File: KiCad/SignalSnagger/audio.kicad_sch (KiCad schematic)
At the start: 36 parts, among them J301 AudioJack4, U301 LM386, U302 LT6231

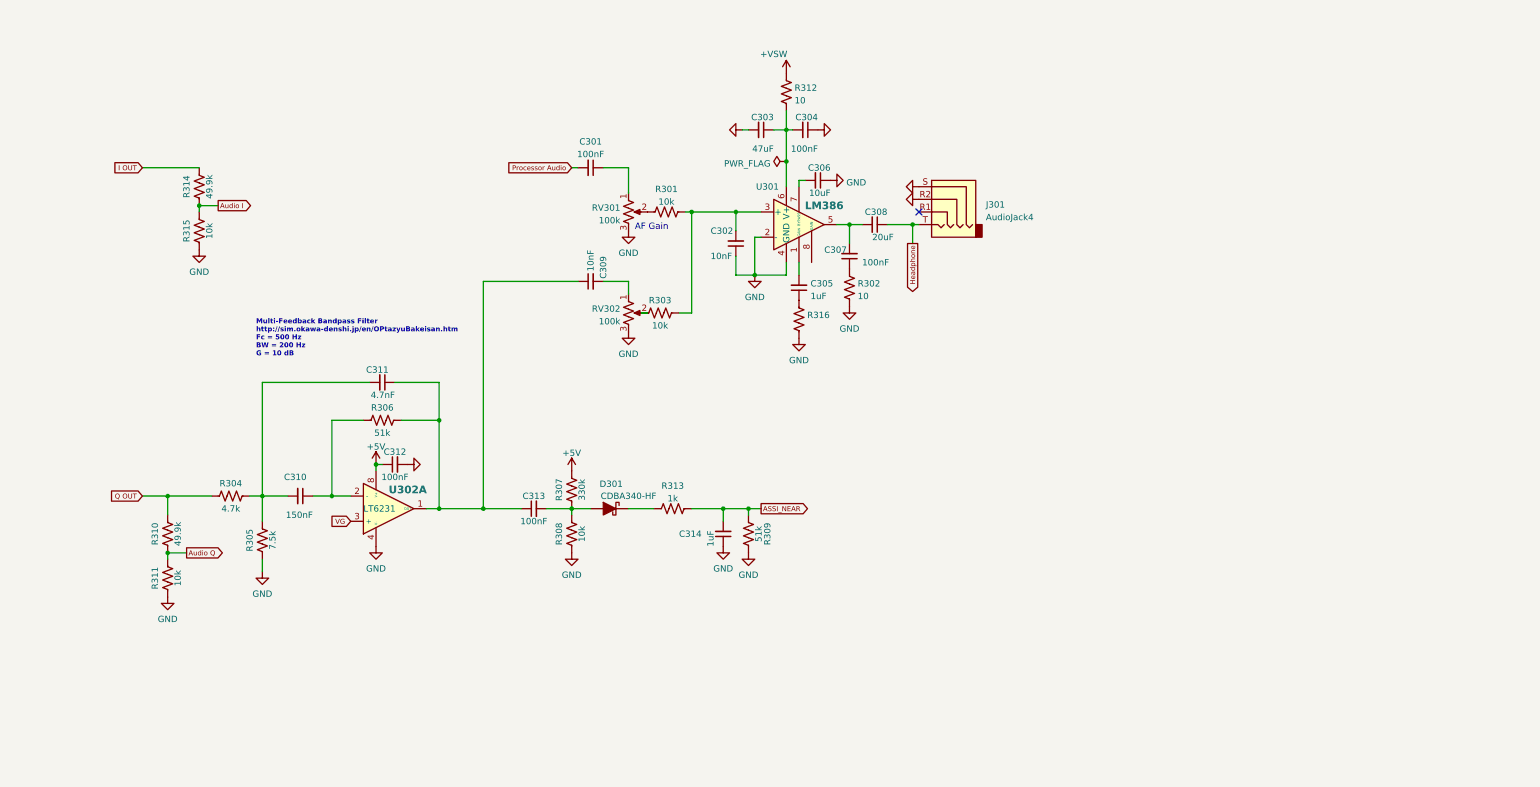
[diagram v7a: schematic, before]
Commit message: Stereo Support
Updates to Audio schematic to reflect discussions regarding stereo support.
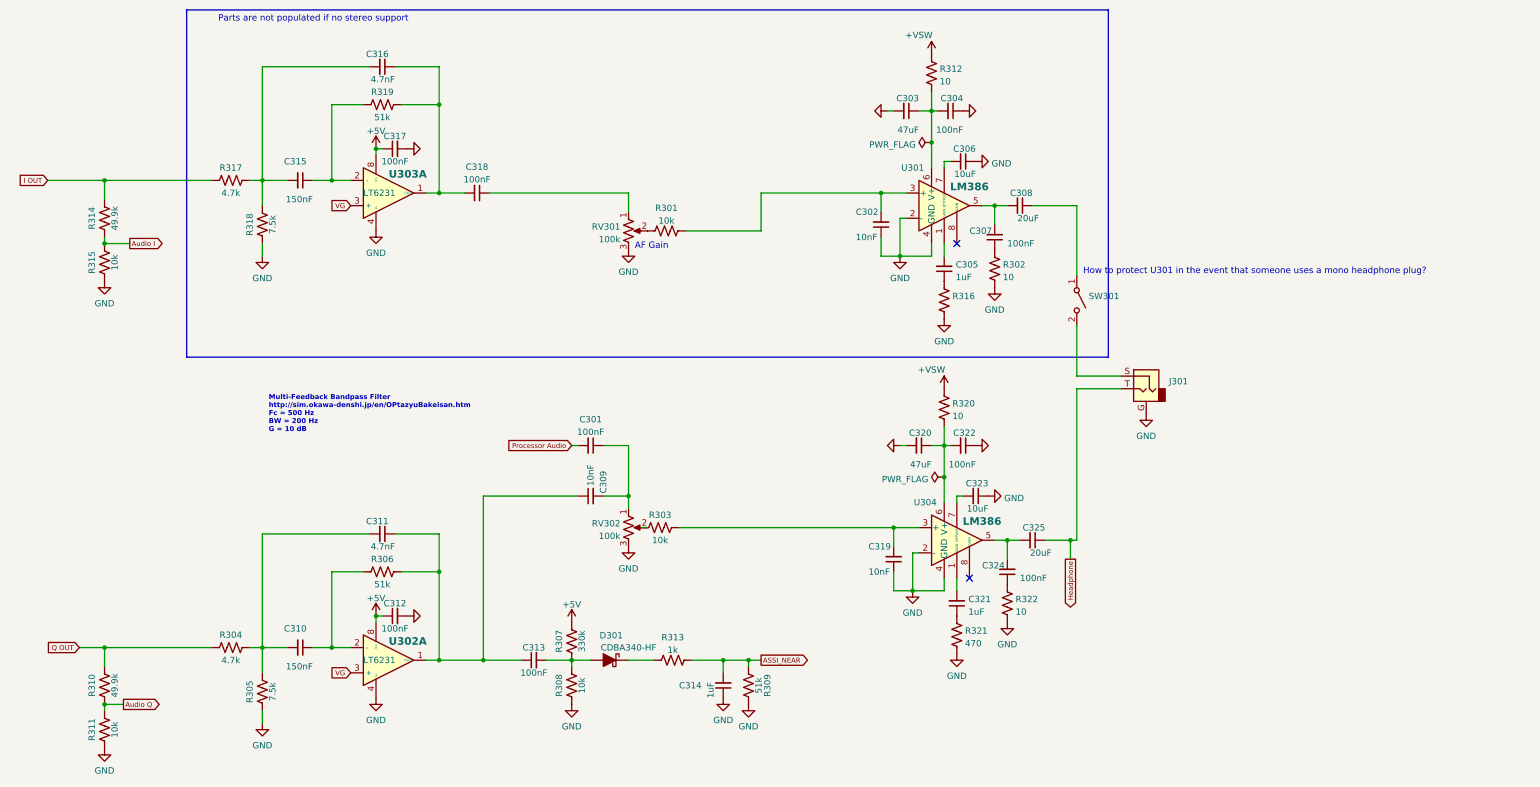
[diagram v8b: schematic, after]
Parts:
- removed J301: AudioJack4, symbol Connector:AudioJack4
- added C315: 150nF, symbol Device:C_Small
- added C316: 4.7nF, symbol Device:C_Small
- added C317, C318, C322, C324: 100nF, symbol Device:C_Small
- added C319: 10nF, symbol Device:C_Small
- added C320: 47uF, symbol Device:C_Small
- added C321: 1uF, symbol Device:C_Small
- added C323: 10uF, symbol Device:C_Small
- added C325: 20uF, symbol Device:C_Small
- added J301: (no value), symbol Connector:AudioJack2_Ground
- added R317: 4.7k, symbol Device:R_US
- added R318: 7.5k, symbol Device:R_US
- added R319: 51k, symbol Device:R_US
- added R320, R322: 10, symbol Device:R_US
- added R321: 470, symbol Device:R_US
- added SW301: (no value), symbol Switch:SW_SPST
- added U303: LT6231, Package_TO_SOT_SMD:TSOT-23-6, symbol Amplifier_Operational:LT6231
- added U304: LM386, symbol Amplifier_Audio:LM386
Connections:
- net +5V: now also C317.1, U303.8 (V+)
- net +VSW: now also R320.1
- net GND: now also C317.2, C319.1, C320.2, C322.1, C323.1, J301.G, R318.2, R321.2, R322.2, U303.4 (V-), U304.2 (-), U304.4 (GND)
- net Headphone: now also C325.1, J301.T; no longer C308.1
- net I OUT: now also R317.1
- net VG: now also U303.3 (+)
- net at C302.2, R301.2, U301.3 (+): no longer R303.2
- net at RV301.1: now also C318.1; no longer C301.1
- net at C309.2, RV302.1: now also C301.1
- new net: C324.1, R322.1
- new net: C324.2, C325.2, U304.5
- new net: C316.1, C318.2, R319.2, U303.1 (OUT)
- new net: C320.1, C322.2, R320.2, U304.6 (V+)
- new net: C315.2, C316.2, R317.2, R318.1
- new net: C321.2, U304.1 (GAIN)
- new net: C319.2, R303.2, U304.3 (+)
- new net: C323.2, U304.7 (BYPASS)
- new net: C315.1, R319.1, U303.2 (-)
- new net: C308.1, SW301.1 (A)
- new net: J301.S, SW301.2 (B)
- new net: C321.1, R321.1
- no-connect marks 1 -> 2
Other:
- note added: "How to protect U301 in the event that someone uses a mono headphone plug?"
- note added: "Parts are not populated if no stereo support"
- moved on the sheet: C301, C302, C303, C304, C305, C306, C307, C308, C309, C310, C311, C312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
